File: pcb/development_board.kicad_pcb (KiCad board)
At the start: 4 copper layers, 74.1 x 24 mm, 29 parts, among them J1 Conn_01x06, J2 TYPE-C-31-M-12, J3 Conn_01x08, J4 Conn_02x09_Top_Bottom, J5 Conn_02x09_Top_Bottom, J6 Conn_02x09_Top_Bottom, J7 Conn_02x09_Top_Bottom, J8 Conn_02x09_Top_Bottom, SW1 SW_DFU, SW2 SW_RST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

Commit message: fixed labels
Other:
- board text added: "03"
- board text added: "04"
- board text added: "07"
- board text added: "08"
- board text added: "15"
- board text added: "16"
- board text added: "17"
- board text added: "18"
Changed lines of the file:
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@@
 		(layer "Edge.Cuts")
 	)
-	(gr_text "21"
+	(gr_text "03"
 		(at 148.336 119.888 90)
 		(layer "F.SilkS")
@@
 		)
 	)
-	(gr_text "21"
+	(gr_text "15"
 		(at 148.336 107.188 90)
 		(layer "F.SilkS")
@@
 		)
 	)
-	(gr_text "21"
+	(gr_text "16"
 		(at 148.336 109.728 90)
 		(layer "F.SilkS")
@@
 		)
 	)
-	(gr_text "21"
+	(gr_text "17"
 		(at 148.336 112.268 90)
 		(layer "F.SilkS")
@@
 		)
 	)
-	(gr_text "21"
+	(gr_text "18"
 		(at 148.336 114.808 90)
 		(layer "F.SilkS")
@@
 		)
 	)
-	(gr_text "21"
+	(gr_text "08"
 		(at 148.336 117.348 90)
 		(layer "F.SilkS")
@@
 		)
 	)
-	(gr_text "21"
+	(gr_text "07"
 		(at 148.336 104.648 90)
 		(layer "F.SilkS")
@@
 		)
 	)
-	(gr_text "21"
+	(gr_text "04"
 		(at 148.336 102.108 90)
 		(layer "F.SilkS")

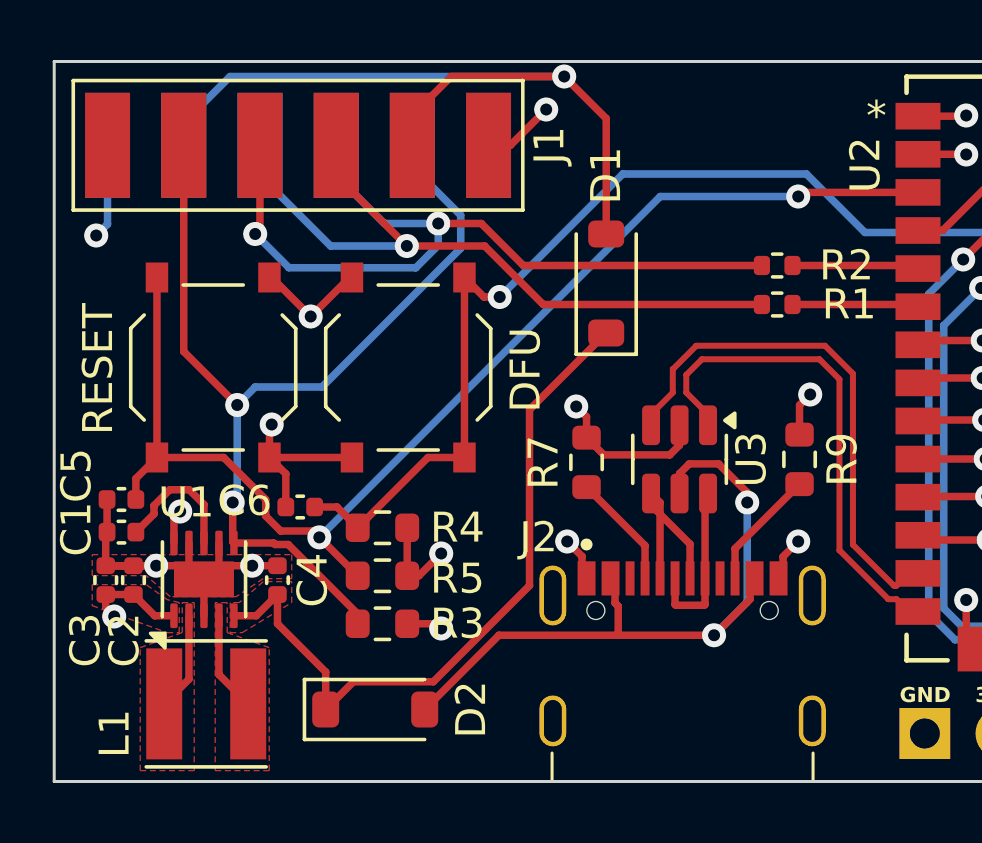
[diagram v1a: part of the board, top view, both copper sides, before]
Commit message: fixed enable when running only on usb
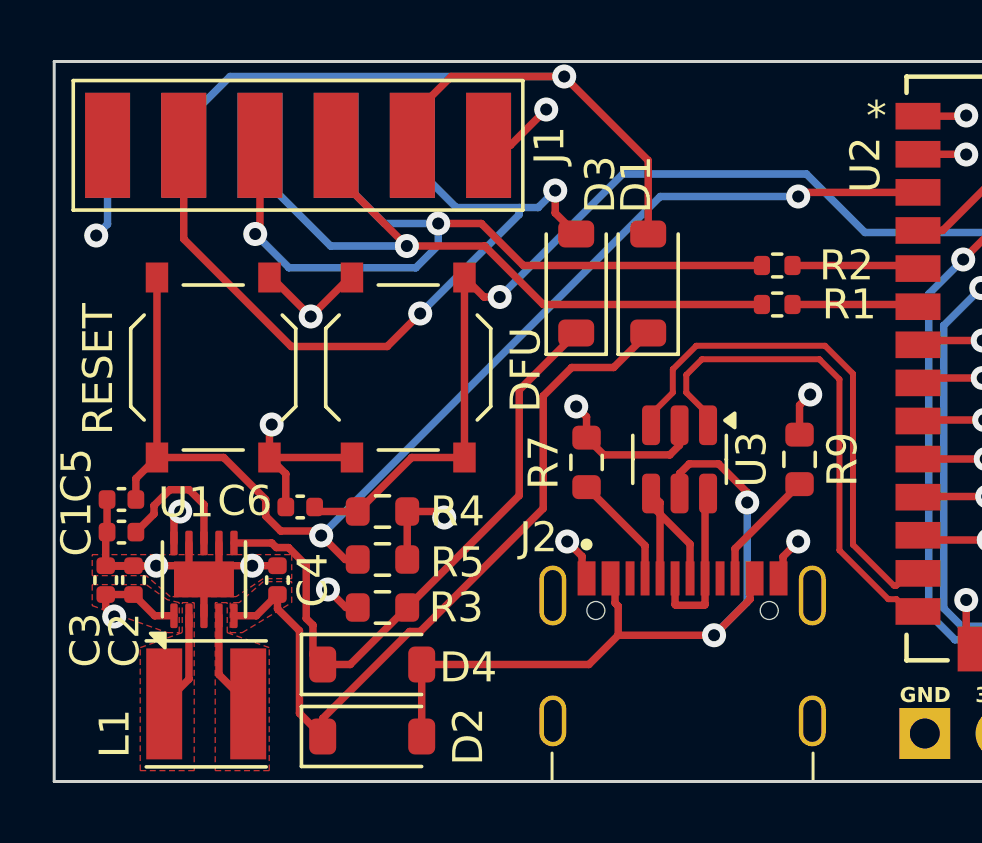
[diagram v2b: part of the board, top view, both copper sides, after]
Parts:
- added D3: LMBR130T1G, Diode_SMD:D_SOD-123, F.Cu at (117.4, 107.4)
- added D4: LMBR130T1G, Diode_SMD:D_SOD-123, F.Cu at (110.6, 120.1)
- moved D1 1.40 mm to (119.8, 107.4)
- moved D2 0.91 mm to (110.6, 122.5)
- moved R3 0.54 mm to (110.9, 118.2), turned to 180 degrees
- moved R4 0.54 mm to (110.9, 115.0)
- moved R5 0.54 mm to (110.9, 116.6)
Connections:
- J1 pad 5: EN -> Net-(D3-A)
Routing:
- net Net-(D3-A): track 0.00 -> 25.8 mm, vias 0 -> 2
- net EN: track 33.2 -> 21.3 mm, vias 2 -> 0
- net Vusb: track 23.7 -> 25.5 mm
- net Net-(D1-K): track 24.2 -> 26.1 mm
- net Vbat: track 26.5 -> 27.1 mm

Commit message: added panelized pcb
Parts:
- added FID1: Fiducial, Fiducial:Fiducial_0.75mm_Mask1.5mm, F.Cu at (125.1, 102.0)
- added FID2: Fiducial, Fiducial:Fiducial_0.75mm_Mask1.5mm, F.Cu at (101.5, 121.1)
- added H1: MountingHole, MountingHole:MountingHole_2mm, F.Cu at (121.5, 102.0)
- added REF**: Tab, PCM_kikit:Tab, F.Cu at (174.3, 112.0)
- added REF**: Tab, PCM_kikit:Tab, F.Cu at (99.8, 112.0)
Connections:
- J2 pad S1: (no net) -> GND
- J2 pad S2: (no net) -> GND
- J2 pad S3: (no net) -> GND
- J2 pad S4: (no net) -> GND
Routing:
- net Vcc: track 9.08 -> 75.7 mm
- net GND: track 48.3 -> 92.0 mm
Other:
- board text added: "BAT"
- board text added: "EN"
- board text added: "SCL"
- board text added: "SDA"
